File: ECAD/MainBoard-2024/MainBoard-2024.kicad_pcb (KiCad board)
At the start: 2 copper layers, 100 x 100 mm, 102 parts, among them J1 XT60, J10 Conn_01x02, J11 Conn_01x03, J12 Conn_01x04, J13 Conn_01x03, J14 Conn_01x03, J15 Conn_01x02, J16 XT30, J17 XT30, J18 Conn_01x02, J2 Conn_01x04, J20 BAU, J21 BAU, J22 Conn_01x04, J23 Conn_01x02, J26 BAU, J27 BAU, J28 Conn_01x02, J29 Conn_01x02, J3 ConStep1, J4 Conn_01x02, J5 ConStep1, J6 ConStep1, J7 XT30, J8 Conn_01x02, J9 Conn_01x02, K2 FINDER-36.11, U1 Teensy3.5_All_Pins, U2 R-78B3.3-2.0, U3 R-78B12-2.0, U4 R-78B5.0-2.0

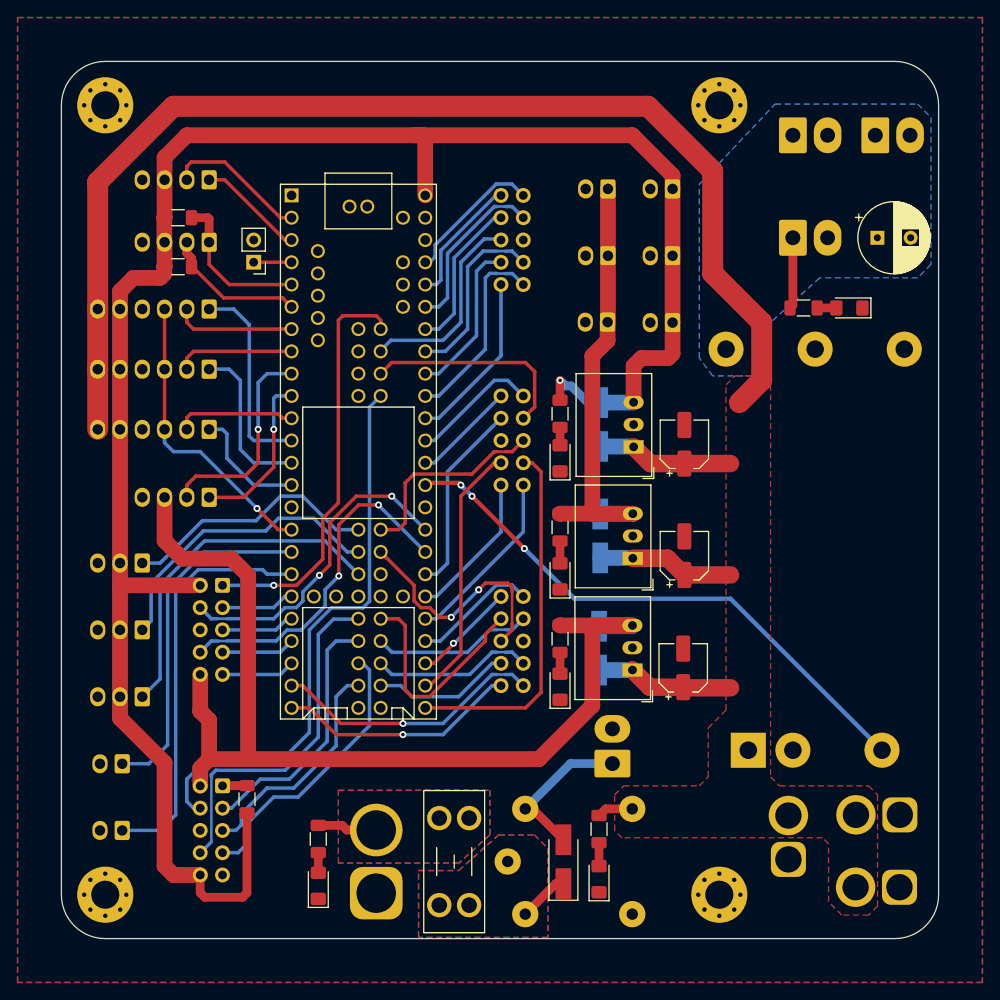
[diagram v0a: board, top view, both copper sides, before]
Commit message: Update Silkscreen
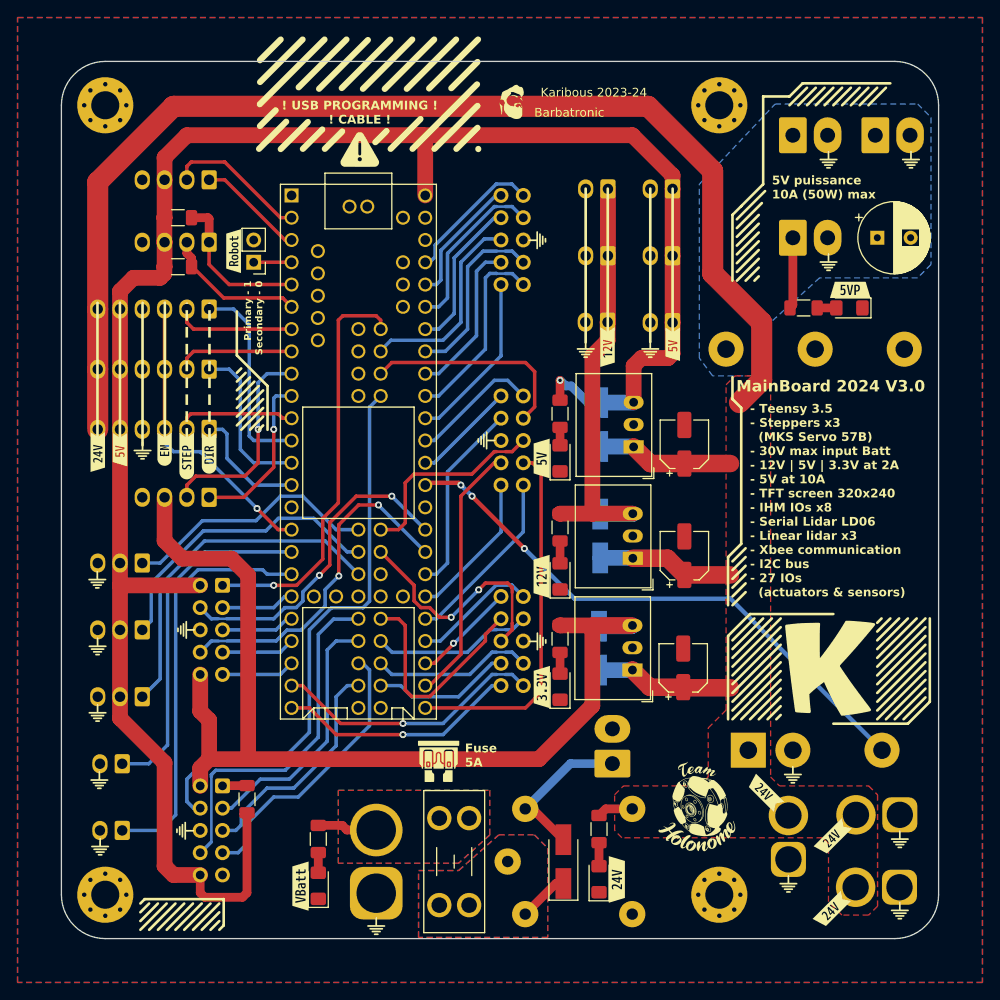
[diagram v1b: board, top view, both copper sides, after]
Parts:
- added G***: LOGO, LOGO, F.Cu at (195.6, 146.8)
- added G***: LOGO, LOGO, F.Cu at (148.4, 93.2)
- added G***: LOGO, LOGO, F.Cu at (114.1, 137.7)
- added G***: LOGO, LOGO, F.Cu at (187.5, 61.2)
- added G***: LOGO, LOGO, F.Cu at (154.3, 116.1)
- added G***: LOGO, LOGO, F.Cu at (109.2, 94.4)
- added G***: LOGO, LOGO, F.Cu at (167.1, 82.8)
- added G***: LOGO, LOGO, F.Cu at (134.0, 60.0)
- added G***: LOGO, LOGO, F.Cu at (104.4, 139.5)
- added G***: LOGO, LOGO, F.Cu at (187.5, 72.9)
- added G***: LOGO, LOGO, F.Cu at (104.3, 131.9)
- added G***: LOGO, LOGO, F.Cu at (183.4, 131.3)
- added G***: LOGO, LOGO, F.Cu at (104.1, 109.1)
- added G***: LOGO, LOGO, F.Cu at (104.1, 116.7)
- added G***: LOGO, LOGO, F.Cu at (196.8, 61.2)
- added G***: LOGO, LOGO, F.Cu at (182.9, 143.8)
- added G***: LOGO, LOGO, F.Cu at (154.3, 70.4)
- added G***: LOGO, LOGO, F.Cu at (114.2, 114.8)
- added G***: LOGO, LOGO, B.Cu at (121.0, 63.6)
- added G***: LOGO, LOGO, F.Cu at (135.9, 148.6)
- added G***: LOGO, LOGO, B.Cu at (120.4, 99.6)
- added G***: LOGO, LOGO, F.Cu at (195.6, 138.7)
- added G***: LOGO, LOGO, F.Cu at (172.5, 135.0)
- added G***: LOGO, LOGO, F.Cu at (151.3, 54.6)
- added G***: LOGO, LOGO, F.Cu at (104.1, 124.3)
- added G***: LOGO, LOGO, F.Cu at (159.8, 82.8)
- added G***: LOGO, LOGO, F.Cu at (143.0, 129.8)
- added kibuzzard-64944345: G***, kibuzzard-64944345, F.Cu at (154.7, 95.3)
- added kibuzzard-6494437E: G***, kibuzzard-6494437E, F.Cu at (154.7, 108.7)
- added kibuzzard-64944398: G***, kibuzzard-64944398, F.Cu at (154.8, 121.3)
- added kibuzzard-649443C2: G***, kibuzzard-649443C2, F.Cu at (189.9, 76.0)
- added kibuzzard-649443DA: G***, kibuzzard-649443DA, F.Cu at (127.3, 144.0)
- added kibuzzard-649443F6: G***, kibuzzard-649443F6, F.Cu at (163.3, 143.3)
- added kibuzzard-6494443F: G***, kibuzzard-6494443F, F.Cu at (119.6, 71.6)
- added kibuzzard-64944CDF: G***, kibuzzard-64944CDF, F.Cu at (111.8, 94.2)
- added kibuzzard-64944CEA: G***, kibuzzard-64944CEA, F.Cu at (114.3, 95.0)
- added kibuzzard-64944CF9: G***, kibuzzard-64944CF9, F.Cu at (116.8, 94.7)
- added kibuzzard-64944D19: G***, kibuzzard-64944D19, F.Cu at (169.7, 82.2)
- added kibuzzard-64944D19: G***, kibuzzard-64944D19, F.Cu at (106.7, 94.3)
- added kibuzzard-64944D37: G***, kibuzzard-64944D37, F.Cu at (187.8, 146.7)
- added kibuzzard-64944D37: G***, kibuzzard-64944D37, F.Cu at (180.2, 133.4)
- added kibuzzard-64944D37: G***, kibuzzard-64944D37, F.Cu at (104.1, 94.5)
- added kibuzzard-64944D37: G***, kibuzzard-64944D37, F.Cu at (187.9, 138.5)
- added kibuzzard-64944DAA: G***, kibuzzard-64944DAA, F.Cu at (162.3, 82.6)
- moved kibuzzard-6493EE56 6.12 mm to (121.5, 81.0)
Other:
- board text added: "! USB PROGRAMMING ! ! CABLE !"
- board text added: "- Teensy 3.5 - Steppers x3 (MKS Servo 57B) - 30V max input Batt - 12V | 5V | 3.3V at 2A - 5V at 10A - TFT screen 320x240 - IHM IOs x8 - Serial Lidar LD06 - Linear lidar x3 - Xbee communication - I2C bus - 27 IOs (actuators & sensors)"
- board text added: "5V puissance 10A (50W) max"
- board text added: "Barbatronic"
- board text added: "Fuse 5A"
- board text added: "Karibous 2023-24"
- board text added: "MainBoard 2024 V3.0"
- board text added: "Primary - 1 Secondary - 0"

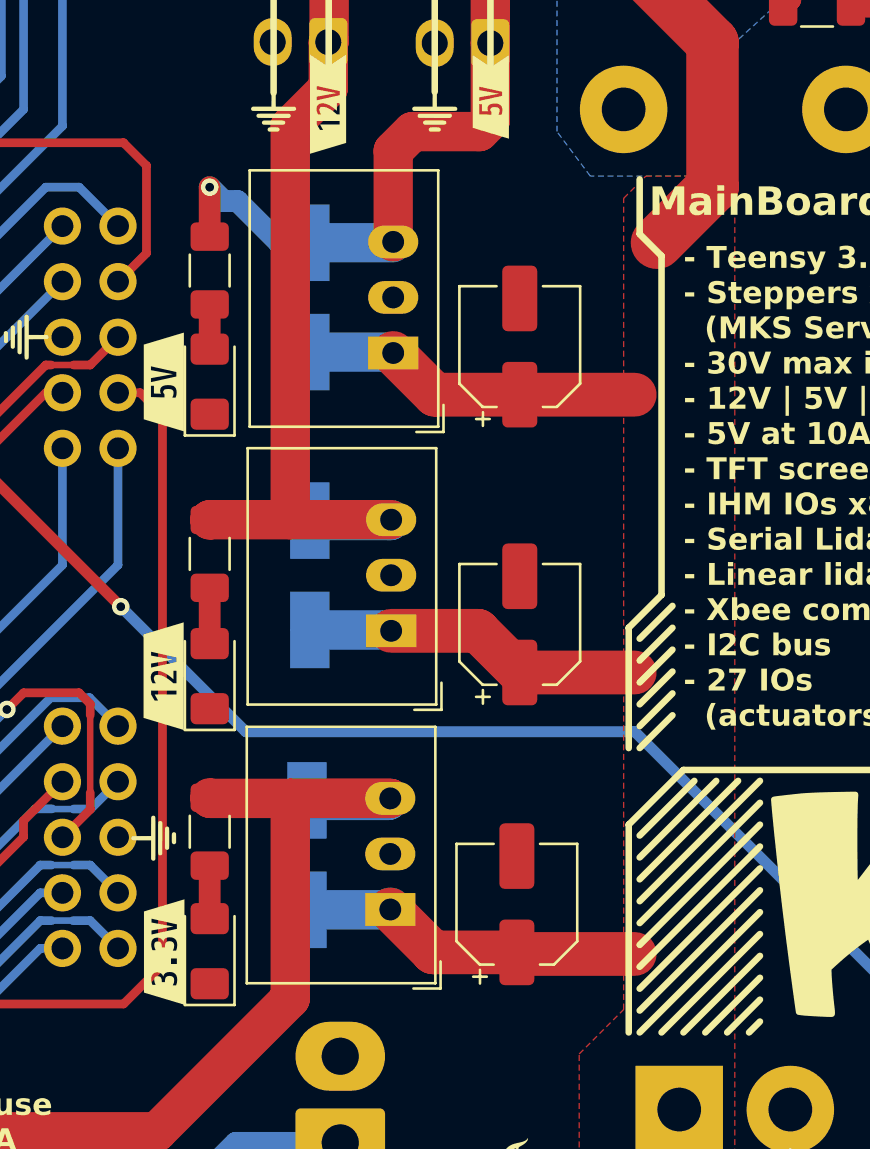
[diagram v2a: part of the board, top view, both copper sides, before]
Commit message: fix recom 78b05 orientation
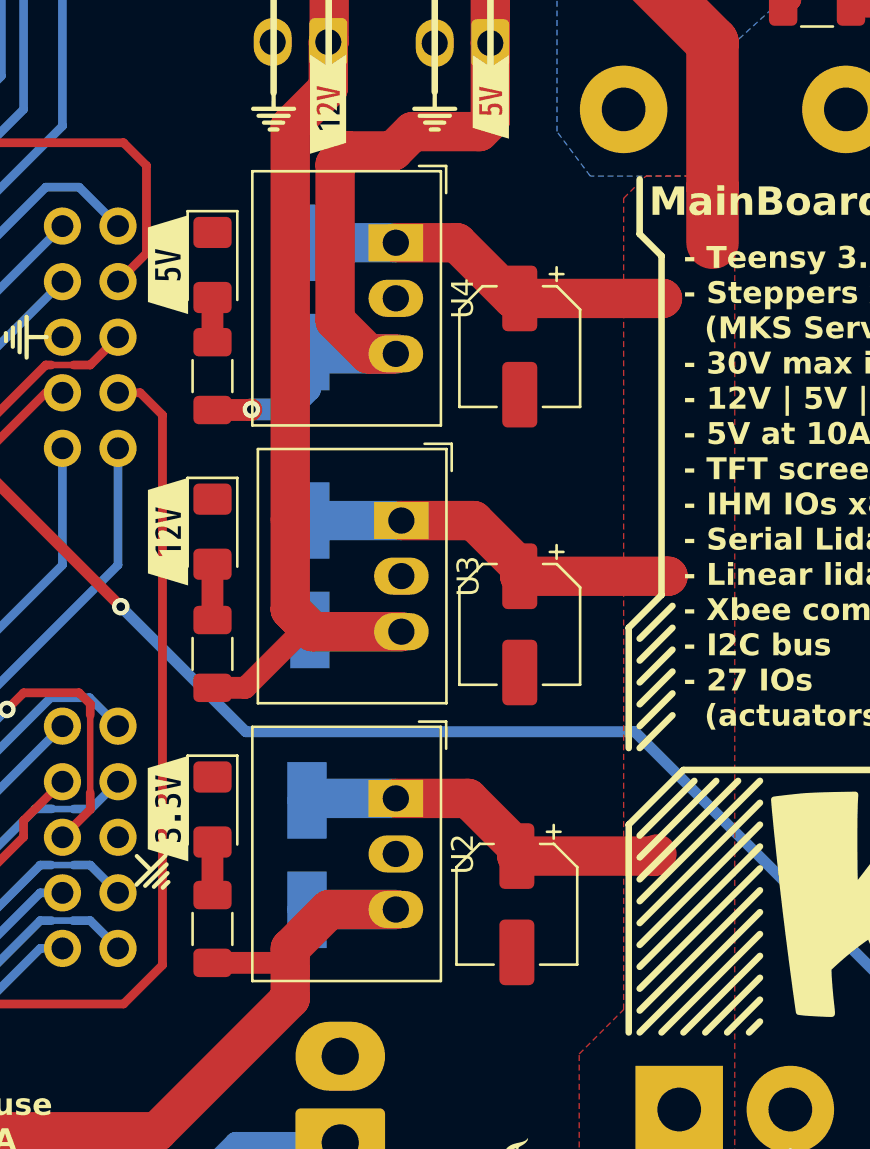
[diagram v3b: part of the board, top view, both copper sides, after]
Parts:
- U2, U3, U4: footprint Converter_DCDC:Converter_DCDC_RECOM_R-78E-0.5_THT -> Converter_DCDC:Converter_DCDC_RECOM_R-78B-2.0_THT
- moved kibuzzard-6494437E 6.61 mm to (154.9, 102.1)
- moved D10 6.61 mm to (157.0, 102.1), turned to -90 degrees
- moved kibuzzard-64944398 6.56 mm to (154.9, 114.8)
- moved D8 6.48 mm to (157.0, 114.8), turned to -90 degrees
- moved kibuzzard-6493EE56 6.38 mm to (121.5, 87.4)
- moved kibuzzard-64944345 5.37 mm to (154.9, 89.9)
- moved D3 5.34 mm to (157.0, 89.9), turned to -90 degrees
- moved U2 5.09 mm to (165.4, 114.3), turned to -90 degrees
- moved U3 5.06 mm to (165.6, 101.6), turned to -90 degrees
- moved U4 5.04 mm to (165.4, 88.9), turned to -90 degrees
- moved R2 4.83 mm to (157.0, 95.0), turned to -90 degrees
- moved R5 4.57 mm to (157.0, 107.7), turned to -90 degrees
- moved R17 4.45 mm to (157.0, 120.3), turned to -90 degrees
- moved G*** 1.49 mm to (154.2, 117.6), turned to 45 degrees
- turned C1 to -90 degrees
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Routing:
- net +3V3: track 122.7 -> 112.5 mm
- net +12V: track 49.8 -> 58.1 mm
- net +5V: track 227.4 -> 235.5 mm
- net +24V: track 186.0 -> 190.1 mm

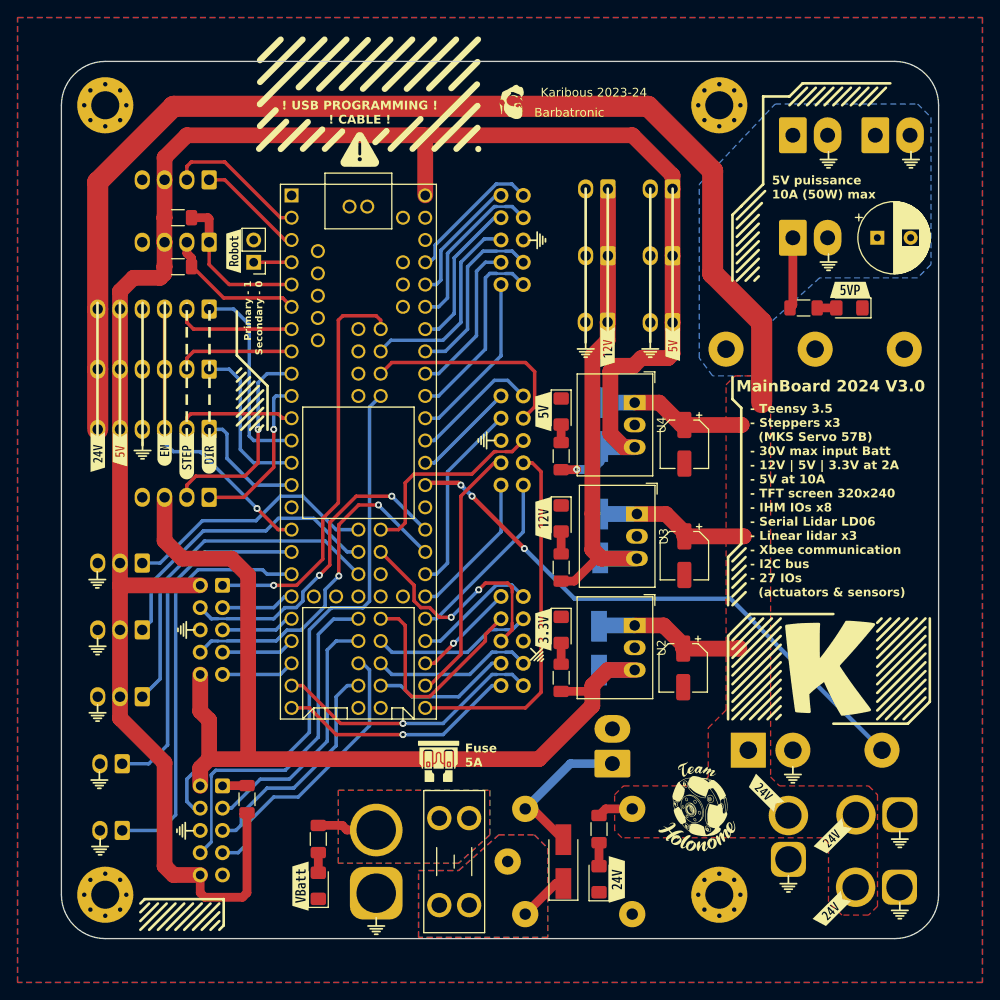
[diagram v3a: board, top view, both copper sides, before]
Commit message: fix gap on recom - Add vias
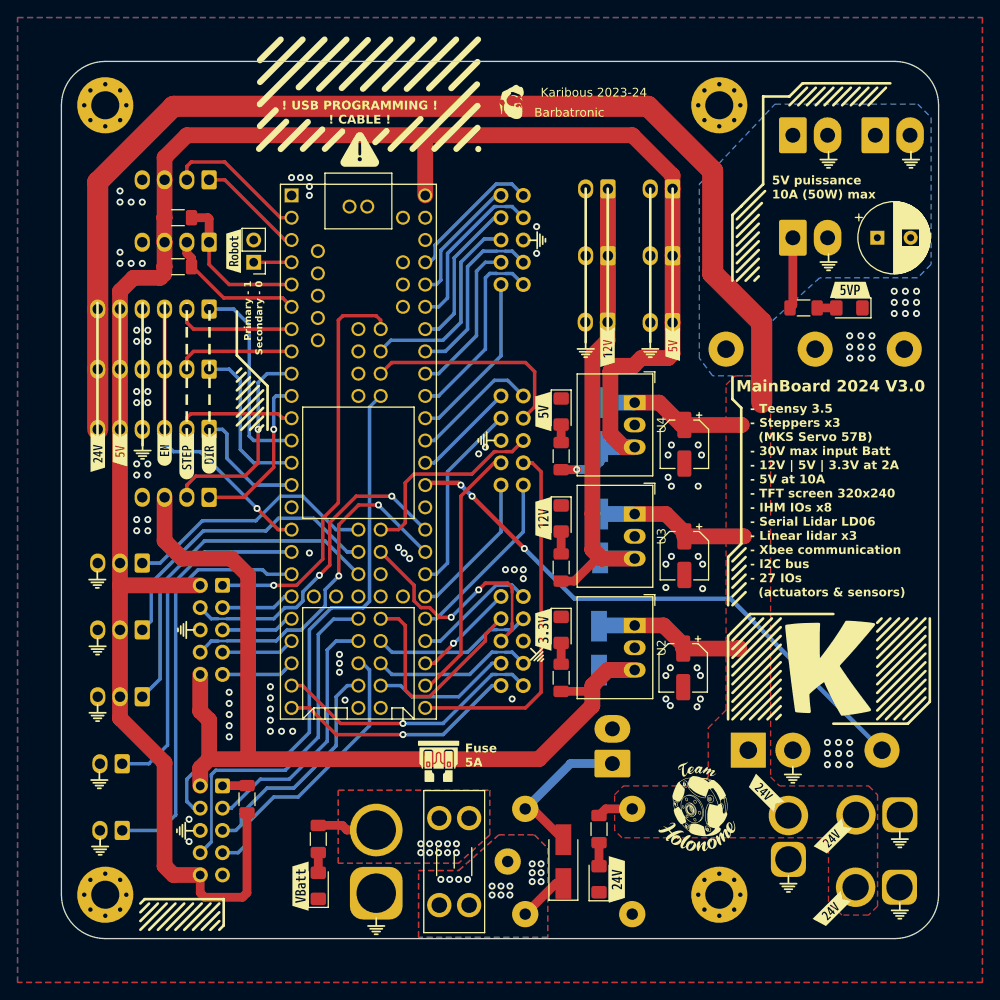
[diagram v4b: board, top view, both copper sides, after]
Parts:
- moved U3 0.25 mm to (165.4, 101.6)
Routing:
- net GND: vias 0 -> 108
- net /24VD: vias 0 -> 16
- net +BATT: vias 0 -> 10
